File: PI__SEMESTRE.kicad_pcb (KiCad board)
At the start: 2 copper layers, 32 parts, among them IC1 LMV358IDR, J1 CX90B-16P1, U1 AMS1117, U11 ESP32-S3-WROOM-1, U14 BME688, U9 GUVA-S12SD

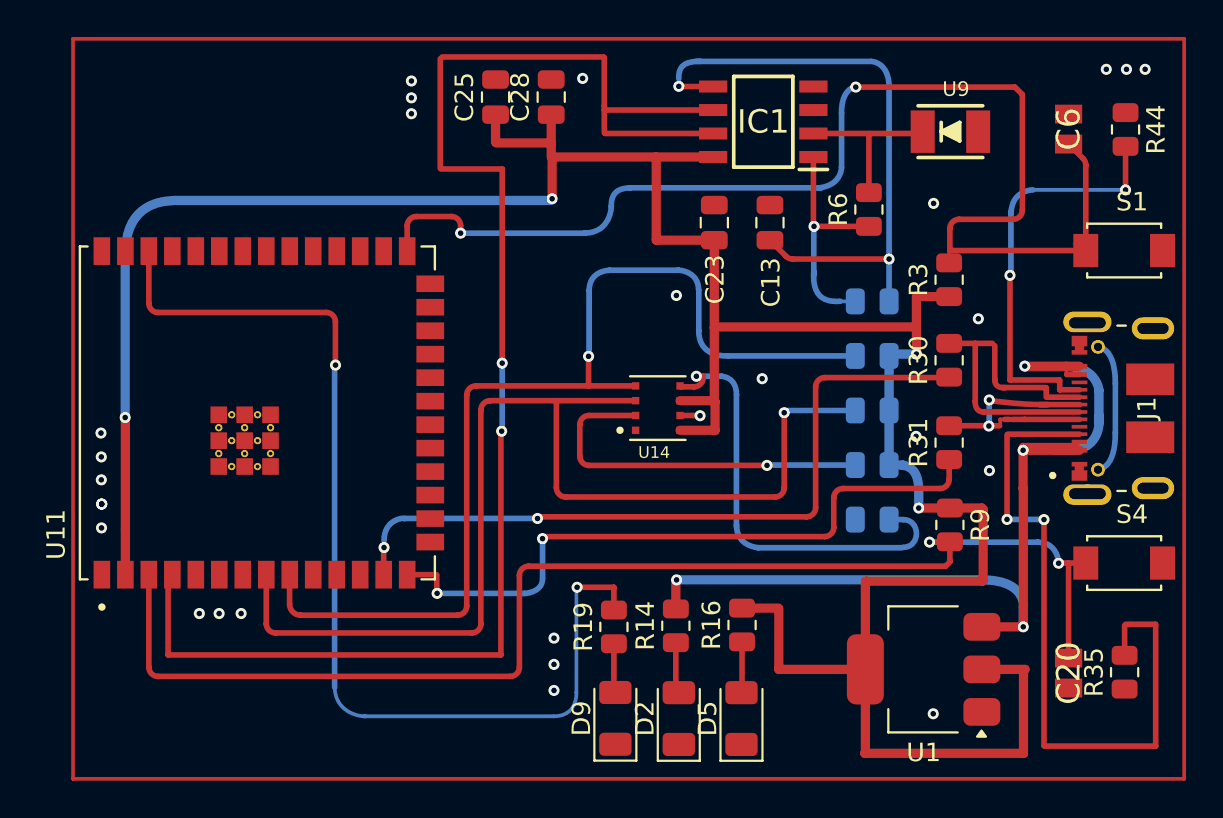
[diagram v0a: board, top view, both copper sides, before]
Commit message: se termino de verificar las pistas, su anchor y se corrigió la curva de las pistas
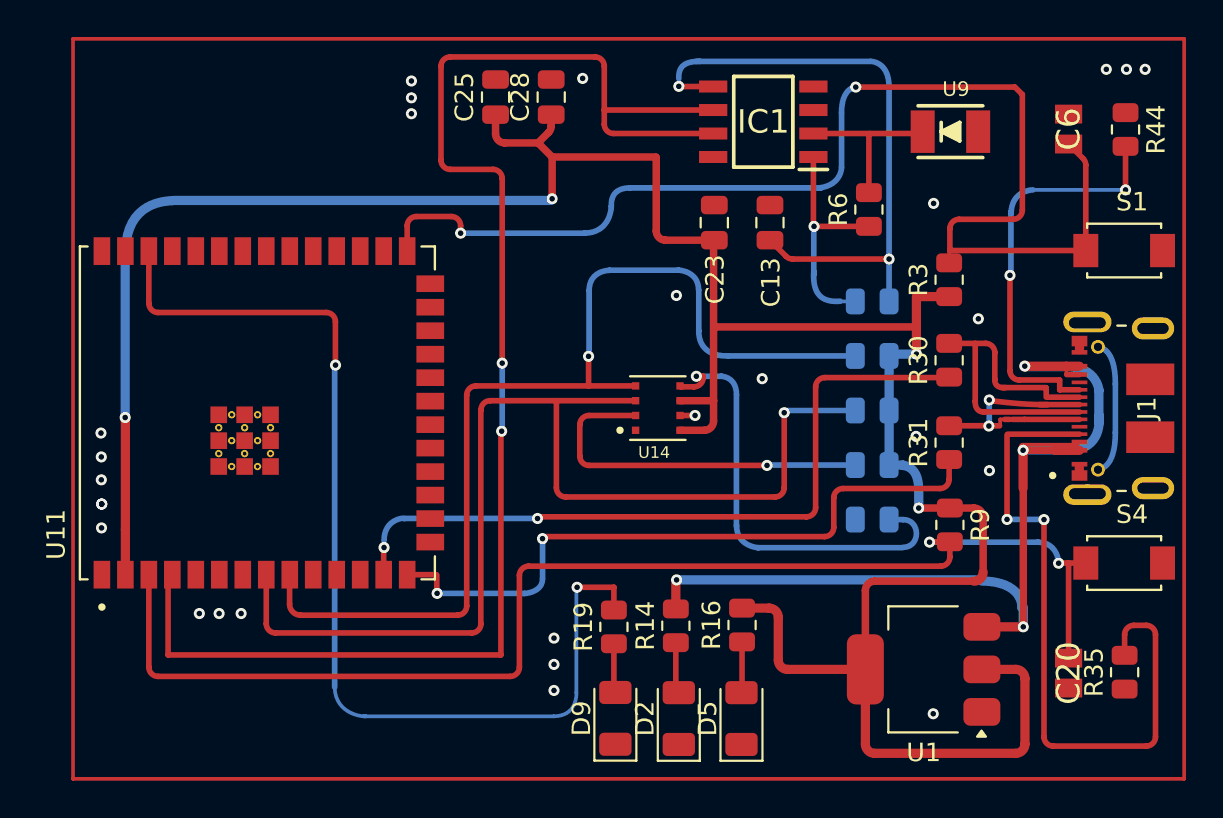
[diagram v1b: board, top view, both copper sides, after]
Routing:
- net +3.3V: track 151.3 -> 148.3 mm
- net +5V: track 47.9 -> 49.9 mm
- net ADC ESP32: track 48.6 -> 47.2 mm
- net Net-(J1-CC1): track 38.7 -> 37.7 mm

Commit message: se corrigen las pistas del usb-c, se corrigen las pistas azules a rectas a 45 grados.
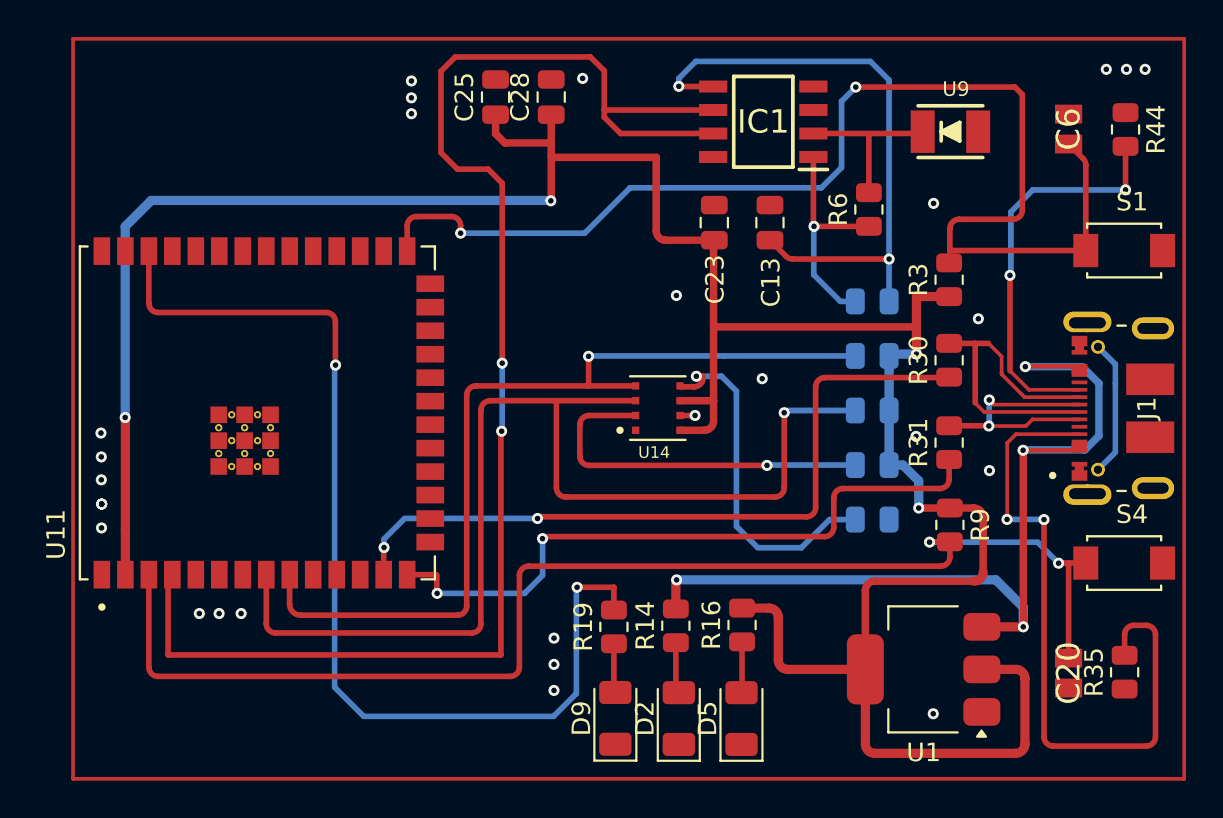
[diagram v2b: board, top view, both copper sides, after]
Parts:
- turned R37 to 0 degrees
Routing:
- net Boot: track 60.6 -> 67.3 mm
- net +3.3V: track 148.3 -> 154.7 mm
- net Net-(J1-MID_PLATE-PadMID1): track 2.65 -> 7.42 mm
- net GPIO2: track 52.5 -> 56.6 mm
- net Filtro: track 30.1 -> 33.3 mm
- net D+: track 11.3 -> 13.9 mm
- net Net-(IC1-OUT): track 10.2 -> 12.3 mm
- net I2C_SCL: track 50.6 -> 48.6 mm
- net +5V: track 49.9 -> 51.7 mm
- net EN: track 68.7 -> 70.4 mm
- net Net-(U11-USB_D-): track 38.5 -> 40.1 mm
- net Net-(J1-CC2): track 20.5 -> 21.9 mm
- net ADC ESP32: track 47.2 -> 46.0 mm
- net Net-(U11-USB_D+): track 35.0 -> 36.2 mm
- net D-: track 17.2 -> 18.0 mm

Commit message: se corrigio anchor de unas pistas y su angulo a 45 grados
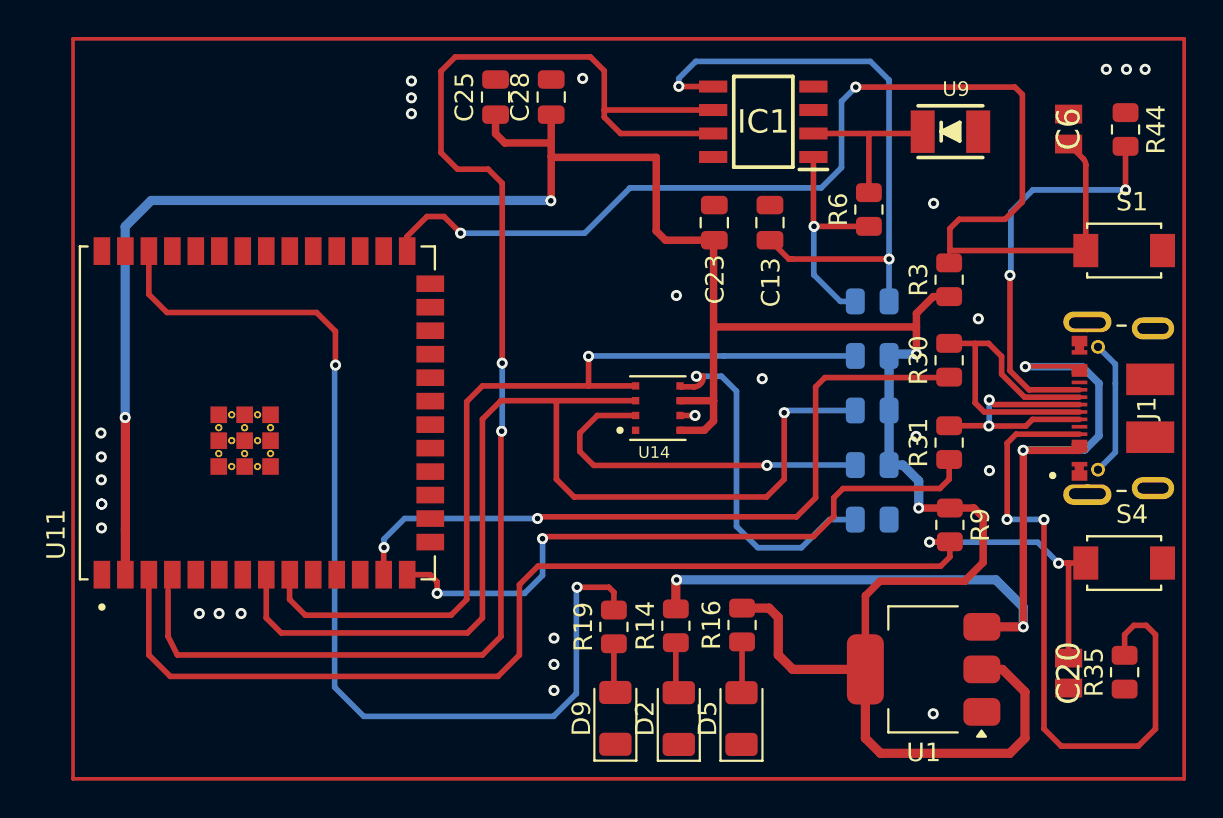
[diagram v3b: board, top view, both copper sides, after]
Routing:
- net +3.3V: track 154.7 -> 152.1 mm
- net I2C_SDA: track 60.5 -> 59.1 mm
- net EN: track 70.4 -> 69.1 mm
- net Boot: track 67.3 -> 66.2 mm
- net GPIO2: track 56.6 -> 55.7 mm
- net I2C_SCL: track 48.6 -> 47.9 mm
- net Net-(J1-CC1): track 37.4 -> 36.7 mm
- net Net-(U11-USB_D+): track 36.2 -> 35.5 mm
- net Net-(U14-CSB): track 20.2 -> 19.6 mm

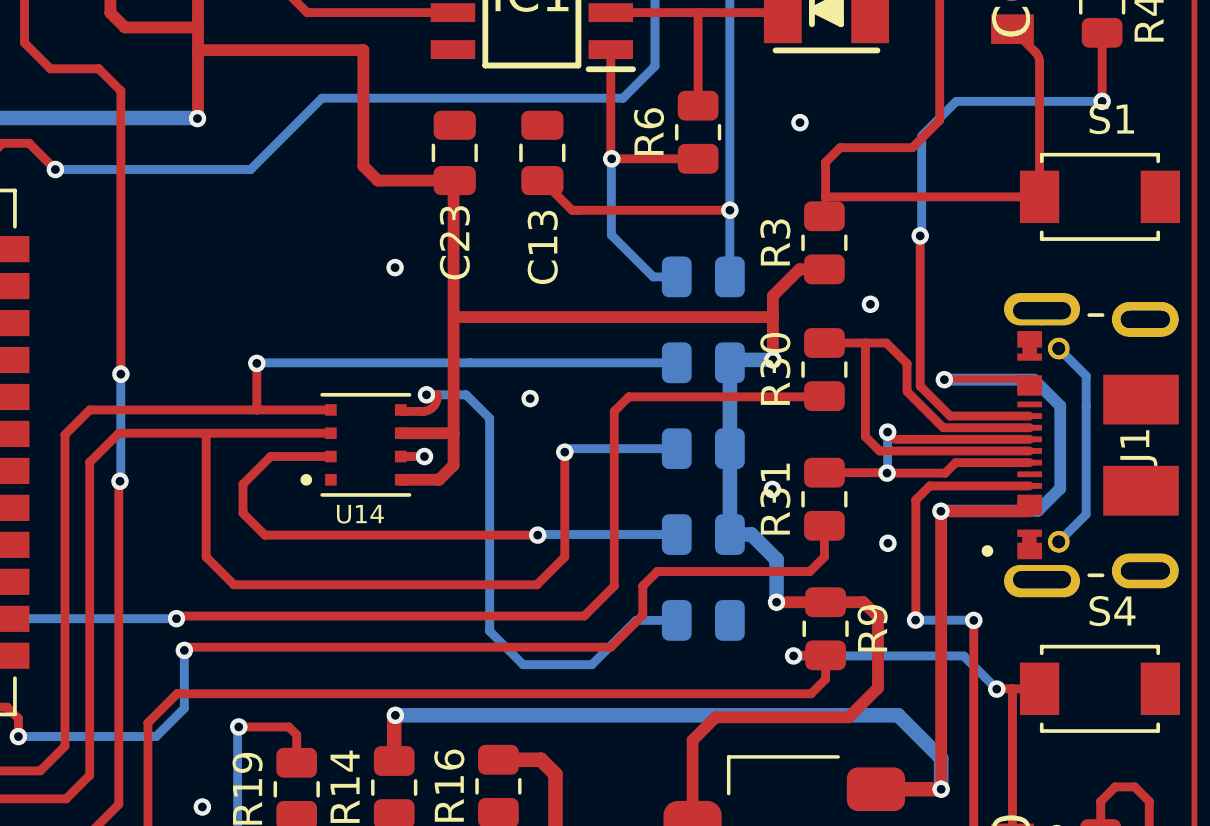
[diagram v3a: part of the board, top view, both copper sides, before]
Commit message: se corrigio el angulo y el ancho de las pistas que faltaban
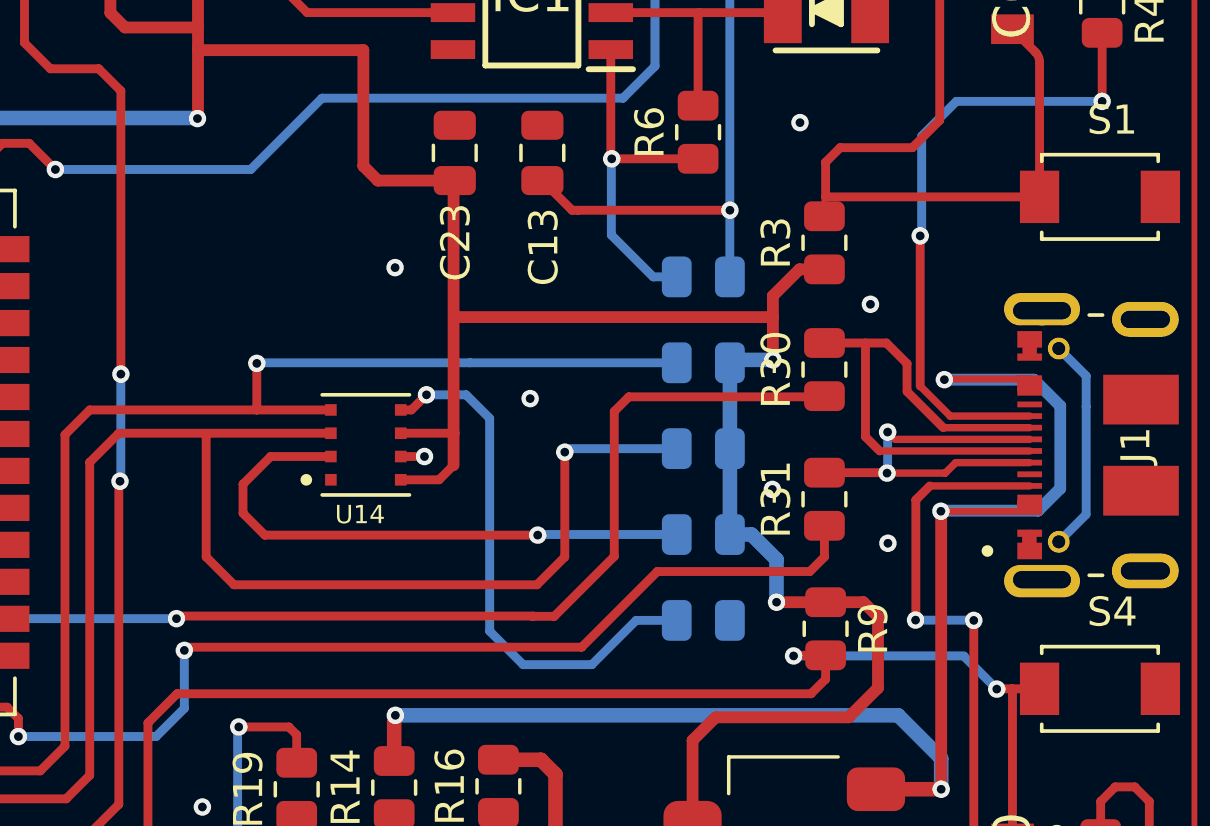
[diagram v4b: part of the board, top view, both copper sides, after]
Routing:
- net Net-(U14-SDO): track 19.3 -> 18.5 mm
- net Net-(U11-USB_D+): track 35.5 -> 34.9 mm
- net Net-(U11-USB_D-): track 39.6 -> 39.1 mm
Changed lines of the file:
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@@
+	)
+	(segment
+		(start 103.54 69.07)
+		(end 103.5 69.11)
+		(width 0.4064)
+		(layer "F.Cu")
+		(net "+3.3V")
 	)
 	(segment
@@
 		(start 103 79.35)
 		(end 103.5 78.85)
-		(width 0.4064)
-		(layer "F.Cu")
-		(net "+3.3V")
-	)
-	(segment
-		(start 103.5 69.11)
-		(end 103.54 69.07)
-		(width 0.4064)
+		(width 0.305)
 		(layer "F.Cu")
 		(net "+3.3V")
@@
 	)
 	(segment
-		(start 103.5 77.75)
-		(end 103.5 69.11)
+		(start 103.5 69.11)
+		(end 103.5 77.75)
 		(width 0.4064)
 		(layer "F.Cu")
@@
 		(start 101.685 77.75)
 		(end 103.5 77.75)
-		(width 0.4064)
+		(width 0.305)
 		(layer "F.Cu")
 		(net "+3.3V")
@@
 		(start 101.685 79.35)
 		(end 103 79.35)
-		(width 0.4064)
+		(width 0.305)
 		(layer "F.Cu")
 		(net "+3.3V")
@@
 	)
 	(segment
-		(start 109.02 83)
-		(end 107.99 84.03)
-		(width 0.305)
-		(layer "F.Cu")
-		(net "Net-(U11-USB_D-)")
-	)
-	(segment
 		(start 116.215 76.5)
 		(end 109.52 76.5)
@@
 	)
 	(segment
+		(start 109.02 81.98)
+		(end 106.96 84.04)
+		(width 0.305)
+		(layer "F.Cu")
+		(net "Net-(U11-USB_D-)")
+	)
+	(segment
 		(start 109.02 77)
-		(end 109.02 83)
+		(end 109.02 81.98)
 		(width 0.305)
 		(layer "F.Cu")
@@
 	)
 	(segment
-		(start 107.99 84.03)
+		(start 106.25 84.03)
 		(end 94.07 84.03)
 		(width 0.305)
@@
 		(end 93.98 84.12)
 		(width 0.2)
+		(layer "F.Cu")
+		(net "Net-(U11-USB_D-)")
+	)
+	(segment
+		(start 106.96 84.04)
+		(end 106.19 84.04)
+		(width 0.305)
 		(layer "F.Cu")
 		(net "Net-(U11-USB_D-)")
@@
 		(start 123.29 78.36)
 		(end 118.137225 78.36)
-		(width 0.305)
+		(width 0.254)
 		(layer "F.Cu")
 		(net "D-")
@@
 		(start 123.29 77.56)
 		(end 120.320068 77.56)
-		(width 0.305)
+		(width 0.254)
 		(layer "F.Cu")
 		(net "D-")
@@
 		(start 123.29 80.435)
 		(end 120.245 80.435)
-		(width 0.4064)
+		(width 0.254)
 		(layer "F.Cu")
 		(net "+5V")
@@
 	)
 	(segment
-		(start 101.735 77)
-		(end 102.4375 77)
+		(start 102.57 76.43)
+		(end 102.05 76.95)
 		(width 0.305)
 		(layer "F.Cu")
@@
 	)
 	(segment
-		(start 102.9375 76.5)
-		(end 102.9375 76.4375)
+		(start 102.05 76.95)
+		(end 101.69 76.95)
 		(width 0.305)
 		(layer "F.Cu")
 		(net "Net-(U14-SDO)")
 	)
-	(segment
-		(start 102.93 76.43)
-		(end 102.57 76.43)
-		(width 0.305)
-		(layer "F.Cu")
-		(net "Net-(U14-SDO)")
-	)
-	(segment
-		(start 101.685 76.95)
-		(end 101.735 77)
-		(width 0.305)
-		(layer "F.Cu")
-		(net "Net-(U14-SDO)")
-	)
-	(segment
-		(start 102.9375 76.4375)
-		(end 102.93 76.43)
-		(width 0.305)
-		(layer "F.Cu")
-		(net "Net-(U14-SDO)")
-	)
 	(via
 		(at 102.57 76.43)
@@
 		(drill 0.3)
 		(layers "F.Cu" "B.Cu")
-		(net "Net-(U14-SDO)")
-	)
-	(arc
-		(start 102.9375 76.5)
-		(mid 102.791053 76.853553)
-		(end 102.4375 77)
-		(width 0.305)
-		(layer "F.Cu")
 		(net "Net-(U14-SDO)")
 	)
@@
 		(start 123.29 79.56)
 		(end 119.86 79.56)
-		(width 0.305)
+		(width 0.254)
 		(layer "F.Cu")
 		(net "Net-(J1-CC1)")
@@
 	)
 	(segment
-		(start 110.5 82.5)
-		(end 110 83)
+		(start 116.24 82)
+		(end 115.74 82.5)
 		(width 0.305)
 		(layer "F.Cu")
@@
 	)
 	(segment
-		(start 108.9 85.1)
+		(start 107.9 85.1)
 		(end 94.36 85.1)
+		(width 0.305)
+		(layer "F.Cu")
+		(net "Net-(U11-USB_D+)")
+	)
+	(segment
+		(start 86.93 87.16)
+		(end 88.16 87.16)
+		(width 0.305)
+		(layer "F.Cu")
+		(net "Net-(U11-USB_D+)")
+	)
+	(segment
+		(start 88.55 87.55)
+		(end 88.55 88.17)
 		(width 0.305)
 		(layer "F.Cu")
@@
 	)
 	(segment
-		(start 86.93 87.16)
-		(end 88.16 87.16)
-		(width 0.305)
+		(start 88.53 88.15)
+		(end 88.55 88.17)
+		(width 0.2)
 		(layer "F.Cu")
 		(net "Net-(U11-USB_D+)")
 	)
 	(segment
-		(start 88.55 87.55)
-		(end 88.55 88.17)
-		(width 0.305)
-		(layer "F.Cu")
-		(net "Net-(U11-USB_D+)")
-	)
-	(segment
-		(start 116.24 82)
-		(end 115.74 82.5)
-		(width 0.305)
+		(start 94.36 85.1)
+		(end 94.25 85.21)
+		(width 0.2)
 		(layer "F.Cu")
 		(net "Net-(U11-USB_D+)")
@@
 	)
 	(segment
-		(start 88.53 88.15)
-		(end 88.55 88.17)
-		(width 0.2)
-		(layer "F.Cu")
-		(net "Net-(U11-USB_D+)")
-	)
-	(segment
-		(start 110 83)
-		(end 110 84)
-		(width 0.305)
-		(layer "F.Cu")
-		(net "Net-(U11-USB_D+)")
-	)
-	(segment
-		(start 94.36 85.1)
-		(end 94.25 85.21)
-		(width 0.2)
-		(layer "F.Cu")
-		(net "Net-(U11-USB_D+)")
-	)
-	(segment
-		(start 110 84)
-		(end 108.9 85.1)
+		(start 110.5 82.5)
+		(end 107.9 85.1)
 		(width 0.305)
 		(layer "F.Cu")
@@
 		(start 123.29 77.16)
 		(end 120.56 77.16)
-		(width 0.305)
+		(width 0.254)
 		(layer "F.Cu")
 		(net "Net-(J1-CC2)")
@@
 		(start 120.56 77.16)
 		(end 119.53 76.13)
-		(width 0.305)
+		(width 0.254)
 		(layer "F.Cu")
 		(net "Net-(J1-CC2)")
@@
 	)
 	(segment
-		(start 118.66 77.96)
-		(end 118.41 77.71)
-		(width 0.2)
-		(layer "F.Cu")
-		(net "D+")
-	)
-	(segment
 		(start 120.75 78.76)
 		(end 120.39 79.12)
-		(width 0.305)
+		(width 0.254)
 		(layer "F.Cu")
 		(net "D+")
@@
 		(start 123.29 78.76)
 		(end 120.75 78.76)
-		(width 0.305)
+		(width 0.254)
 		(layer "F.Cu")
 		(net "D+")
@@
 		(start 120.39 79.12)
 		(end 118.41 79.12)
-		(width 0.305)
+		(width 0.254)
 		(layer "F.Cu")
 		(net "D+")
@@
 		(start 123.29 77.96)
 		(end 118.66 77.96)
-		(width 0.305)
+		(width 0.254)
 		(layer "F.Cu")
 		(net "D+")
